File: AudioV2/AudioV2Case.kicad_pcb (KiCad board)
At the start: 2 copper layers, 110 x 110 mm, 265 parts, among them J1601 AUDIO, J1602 V_IN, J1603 15_V_IN, J201 +15/A_GND/-15 out, J202 PD module in (1=GND 2=+12V), Q401 BSS138, Q402 BSS138, SW1601 DEST sense (3PDT 3rd pole, sa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, SW402 PWR SW, SW501 DEST L (PHONE/MUTE/LINE), SW502 DEST R (PHONE/MUTE/LINE), U1601 OPA1656, U1602 OPA1656, U1603 LT1763-3.3, U1605 TPS3307-33, U1606 LT1763-5, U1607 BP5293-50, U1608 OPA1656, U1609 XC8107AC20MR-G, U1610 MCP23017 (UI 0x22), U1611 OPA1656, U201 REC20K-2415DZ, U202 L7809CV +9V, U311 TMUX7612, U312 TMUX7612, U402 PT2314E, U403 BP5293-50 +5V, U501 OPA1652, Y1601 ASFL1-12.288MHZ-EC-T

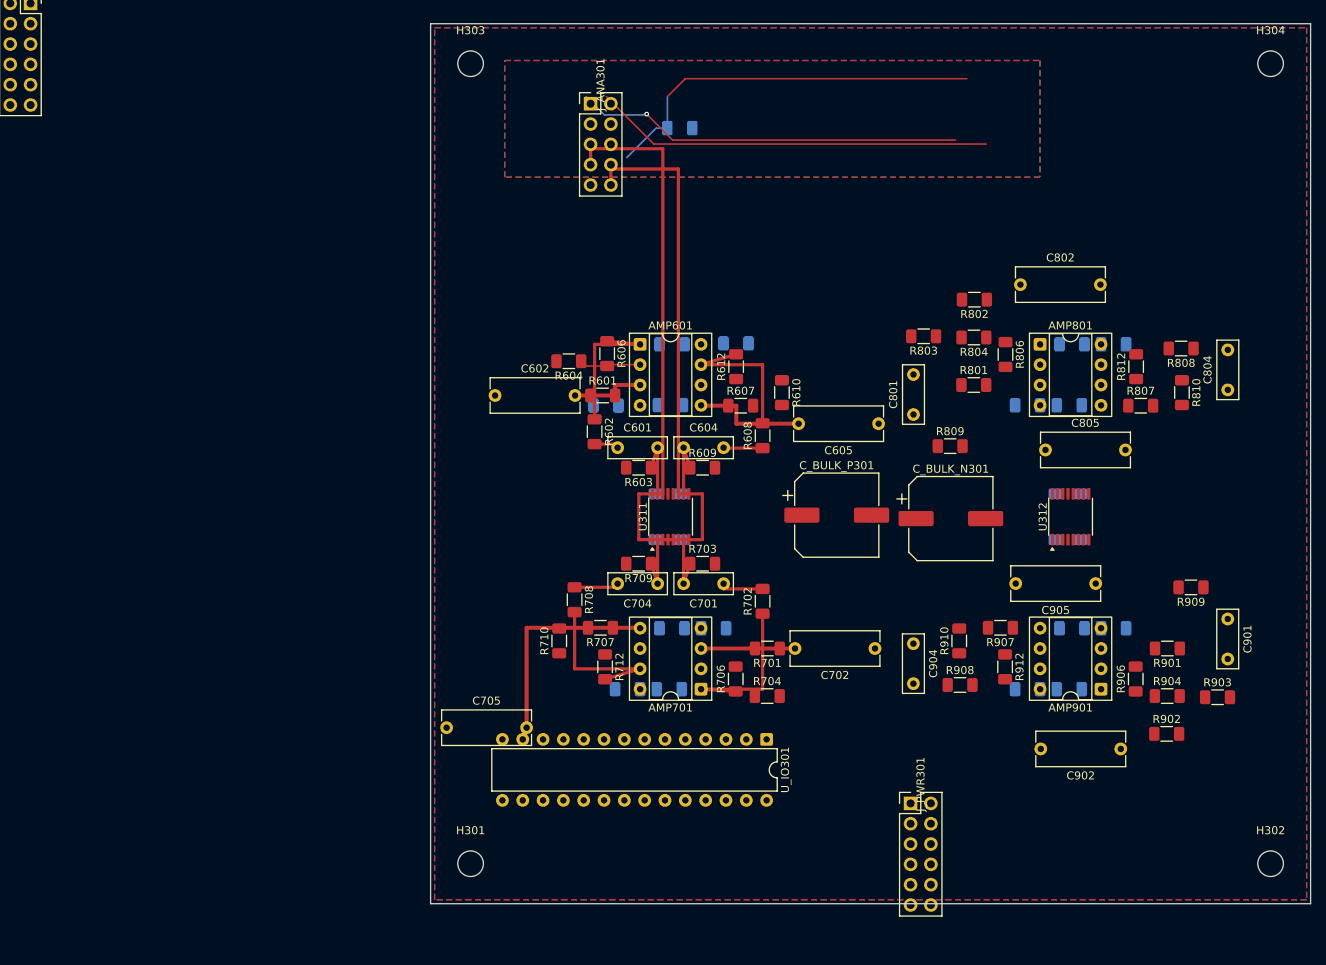
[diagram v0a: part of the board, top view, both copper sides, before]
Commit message: AudioV2: TMUX を 270°（ピン1側=CH1）にし、AmpChannel のスイッチ用デカップを外す
S=各ch出力・D=AMP_SEL に戻し、CH1 配線途中の PCB も取り込む。C607/C610 は D22 の残りなのでシートから削除した。

Co-authored-by: Cursor <cursoragent@cursor.com>
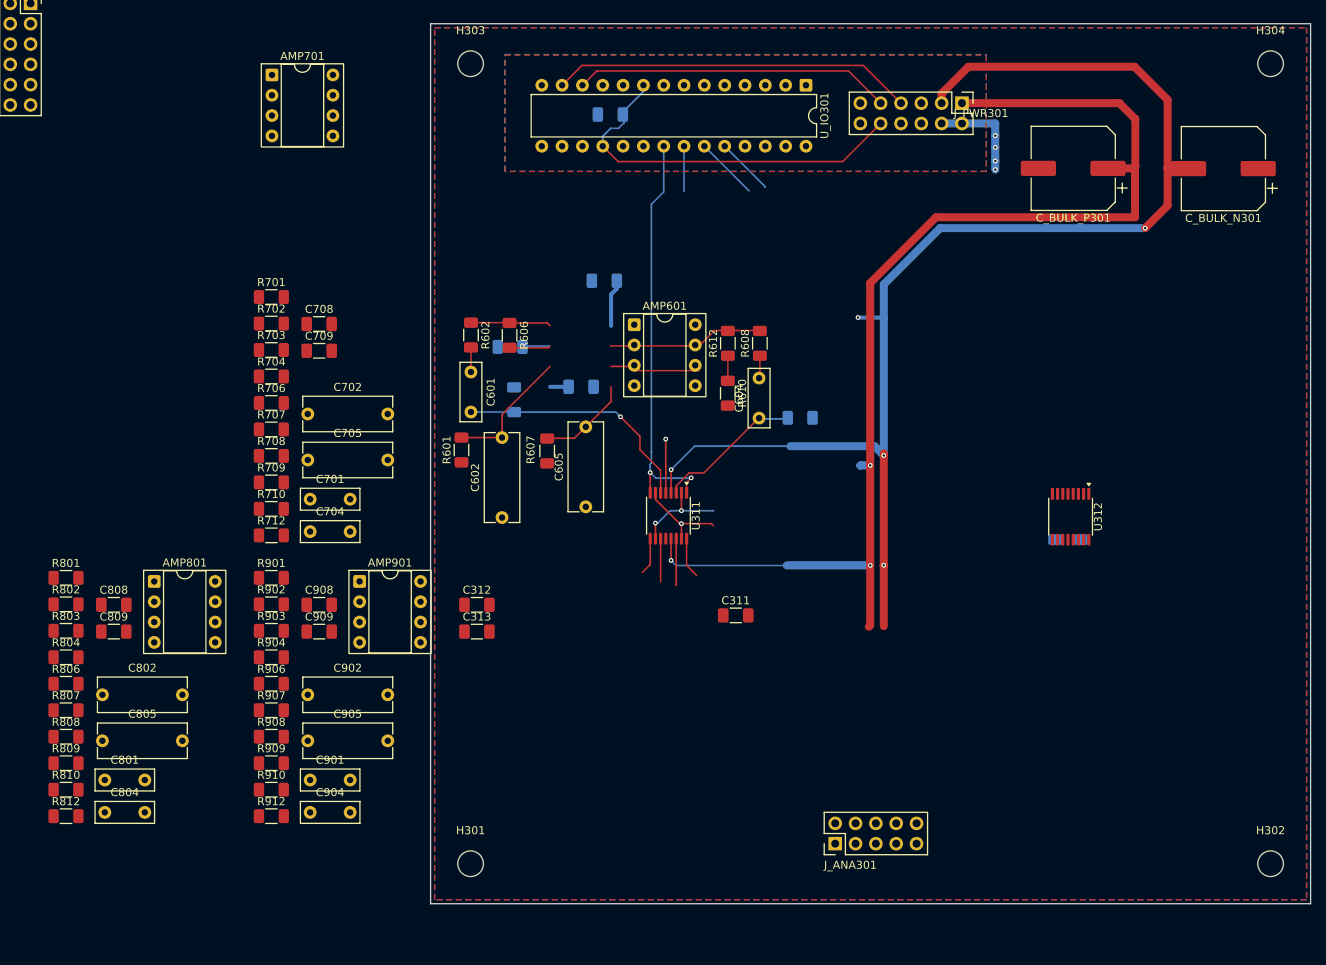
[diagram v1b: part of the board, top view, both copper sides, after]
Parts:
- removed C607, C610, C707, C710, C807, C810, C907, C910: 100nF, Capacitor_SMD:C_1206_3216Metric_Pad1.33x1.80mm_HandSolder
- C311, C312, C313, C708, C709, C808, C809, C908, C909: moved to F.Cu
- R603, R604, R609: moved to B.Cu
- moved C804 150.0 mm to (299.3, 228.6), turned to 0 degrees
- moved R810 148.1 mm to (294.4, 225.7), turned to 0 degrees
- moved R808 147.6 mm to (294.4, 219.1), turned to 0 degrees
- moved R812 145.1 mm to (294.4, 229.1), turned to 0 degrees
- moved R807 139.6 mm to (294.4, 215.8)
- moved C802 125.7 mm to (299.0, 213.9)
- moved R806 124.4 mm to (294.4, 212.5), turned to 0 degrees
- moved C808 124.1 mm to (300.4, 202.6)
- moved C805 123.4 mm to (299.0, 219.6)
- moved R804 120.3 mm to (294.4, 209.2), turned to 0 degrees
- moved R802 119.8 mm to (294.4, 202.6), turned to 0 degrees
- moved R903 118.6 mm to (320.1, 205.9)
- moved C809 117.7 mm to (300.4, 206.0)
- moved R809 117.4 mm to (294.4, 222.4)
- moved R909 117.0 mm to (320.1, 222.4), turned to 0 degrees
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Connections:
- U311 pad 1: /AmpBankSwitch/SEL_CH2 -> /AmpBankSwitch/SEL_CH1
- U311 pad 10: /AmpBankSwitch/CH1_OUT_R -> /AMP_SEL_R
- U311 pad 11: /AMP_SEL_R -> /AmpBankSwitch/CH2_OUT_R
- U311 pad 14: /AMP_SEL_L -> /AmpBankSwitch/CH2_OUT_L
- U311 pad 15: /AmpBankSwitch/CH1_OUT_L -> /AMP_SEL_L
- U311 pad 16: /AmpBankSwitch/SEL_CH1 -> /AmpBankSwitch/SEL_CH2
- U311 pad 2: /AmpBankSwitch/CH2_OUT_R -> /AMP_SEL_R
- U311 pad 3: /AMP_SEL_R -> /AmpBankSwitch/CH1_OUT_R
- U311 pad 6: /AMP_SEL_L -> /AmpBankSwitch/CH1_OUT_L
- U311 pad 7: /AmpBankSwitch/CH2_OUT_L -> /AMP_SEL_L
- U311 pad 8: /AmpBankSwitch/SEL_CH2 -> /AmpBankSwitch/SEL_CH1
- U311 pad 9: /AmpBankSwitch/SEL_CH1 -> /AmpBankSwitch/SEL_CH2
- U312 pad 1: /AmpBankSwitch/SEL_CH4 -> /AmpBankSwitch/SEL_CH3
- U312 pad 10: /AmpBankSwitch/CH3_OUT_R -> /AMP_SEL_R
- U312 pad 11: /AMP_SEL_R -> /AmpBankSwitch/CH4_OUT_R
- U312 pad 14: /AMP_SEL_L -> /AmpBankSwitch/CH4_OUT_L
- U312 pad 15: /AmpBankSwitch/CH3_OUT_L -> /AMP_SEL_L
- U312 pad 16: /AmpBankSwitch/SEL_CH3 -> /AmpBankSwitch/SEL_CH4
- U312 pad 2: /AmpBankSwitch/CH4_OUT_R -> /AMP_SEL_R
- U312 pad 3: /AMP_SEL_R -> /AmpBankSwitch/CH3_OUT_R
- U312 pad 6: /AMP_SEL_L -> /AmpBankSwitch/CH3_OUT_L
- U312 pad 7: /AmpBankSwitch/CH4_OUT_L -> /AMP_SEL_L
- U312 pad 8: /AmpBankSwitch/SEL_CH4 -> /AmpBankSwitch/SEL_CH3
- U312 pad 9: /AmpBankSwitch/SEL_CH3 -> /AmpBankSwitch/SEL_CH4
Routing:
- net /-15V: track 0.00 -> 170.5 mm, vias 0 -> 5
- net /+15V: track 0.00 -> 152.9 mm, vias 0 -> 3
- net /A_GND: track 98.4 -> 19.4 mm, vias 1 -> 5
- net /AMP_SEL_L: track 67.8 -> 11.3 mm, vias 0 -> 1
- net /AMP_SEL_R: track 64.7 -> 12.1 mm, vias 0 -> 2
- net /AmpBankSwitch/SEL_CH1: track 0.00 -> 51.6 mm, vias 0 -> 2
- net /I2C_SDA: track 0.00 -> 45.3 mm
- net /I2C_SCL: track 0.00 -> 39.7 mm
- net Net-(AMP701B-+): track 26.7 -> 0.00 mm
- net /AmpBankSwitch/CH1_OUT_L: track 8.40 -> 30.5 mm, vias 0 -> 1
- net Net-(AMP701-Pad1): track 21.5 -> 0.00 mm
- net Net-(AMP701-Pad7): track 19.8 -> 0.00 mm
- net /AmpBankSwitch/SEL_CH2: track 0.00 -> 15.3 mm
- net Net-(AMP601B--): track 0.00 -> 14.4 mm
- net Net-(AMP701A-+): track 11.7 -> 0.00 mm
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
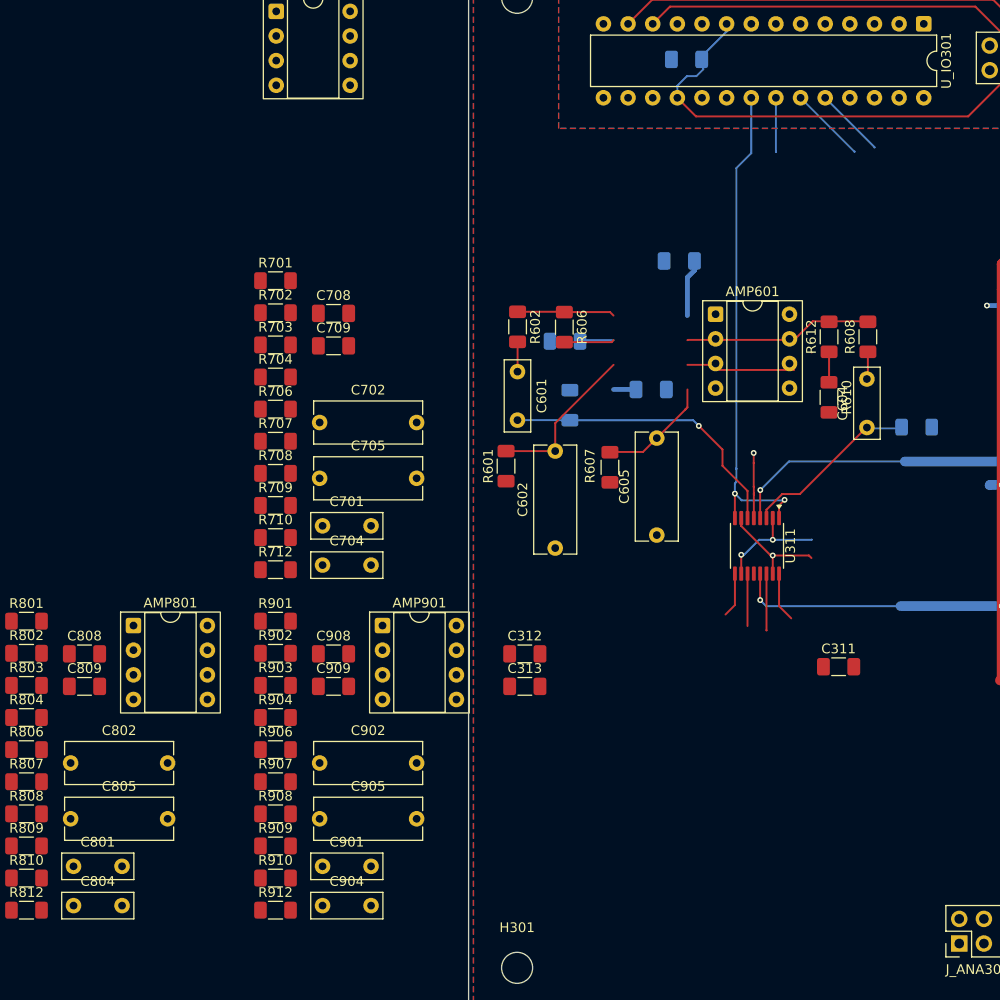
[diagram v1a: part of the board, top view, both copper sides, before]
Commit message: AudioV2: Amp カップリングフィルムを TDK B32529 系統の FP に揃えた
入力1µFは P5/W4.5、出力2.2µFは P5/W7.2。旧 P10 / W2.5 の誤りを直し、PCB も同期。

Co-authored-by: Cursor <cursoragent@cursor.com>
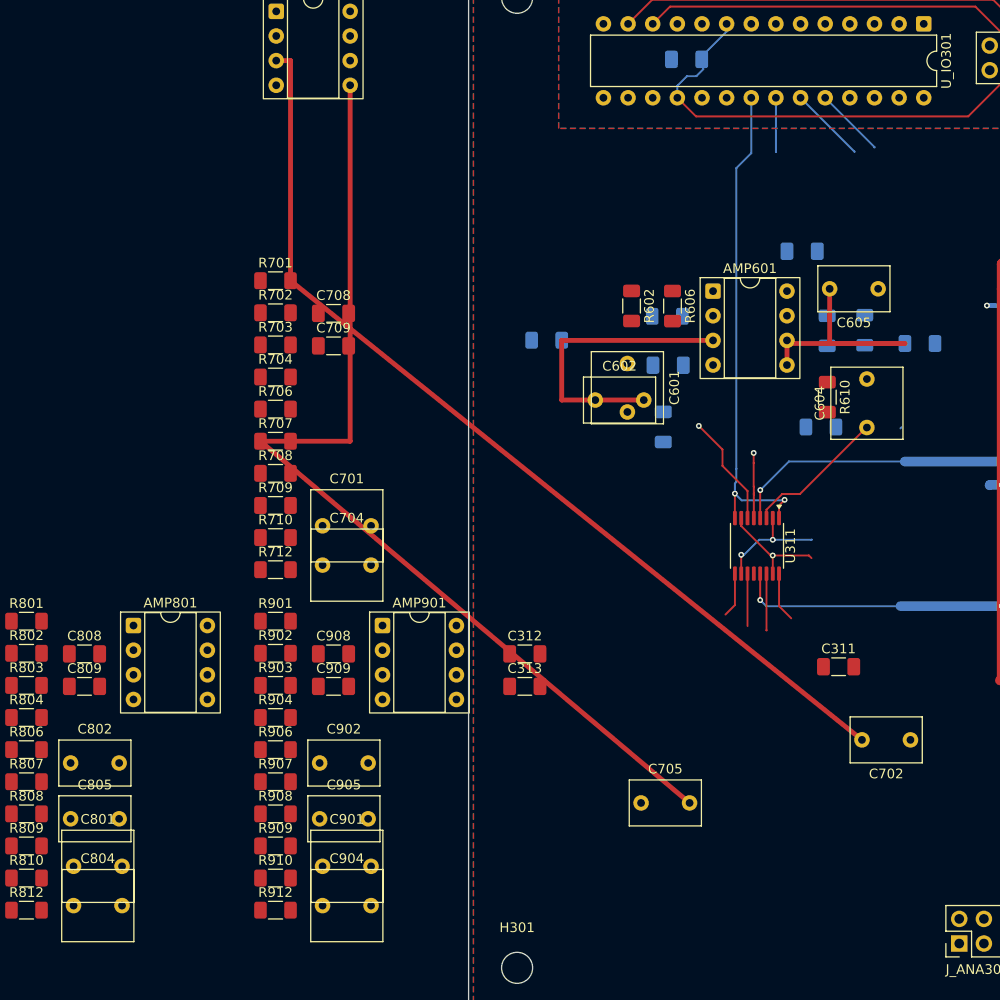
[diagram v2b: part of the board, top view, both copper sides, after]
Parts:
- C601, C604, C701, C704, C801, C804, C901, C904: footprint Capacitor_THT:C_Rect_L7.2mm_W2.5mm_P5.00mm_FKS2_FKP2_MKS2_MKP2 -> C_Rect_L7.2mm_W7.2mm_P5.00mm_FKS2_FKP2_MKS2_MKP2
- C602, C605, C702, C705, C802, C805, C902, C905: footprint Capacitor_THT:C_Rect_L11.0mm_W4.2mm_P10.00mm_MKT -> C_Rect_L7.2mm_W4.5mm_P5.00mm_FKS2_FKP2_MKS2_MKP2
- R601, R607, R608, R612: moved to B.Cu
- moved C702 69.1 mm to (385.6, 211.5), turned to 180 degrees
- moved C705 47.1 mm to (357.8, 218.0)
- moved R607 34.4 mm to (386.5, 170.6), turned to 0 degrees
- moved C605 34.1 mm to (382.2, 165.0), turned to 180 degrees
- moved C602 15.8 mm to (353.1, 176.5), turned to 0 degrees
- moved R601 13.6 mm to (348.1, 170.3), turned to 0 degrees
- moved C608 12.7 mm to (374.4, 161.1), turned to 0 degrees
- moved R602 11.9 mm to (356.8, 166.8)
- moved C601 11.4 mm to (356.4, 172.7)
- moved R606 11.4 mm to (361.0, 166.8)
- moved R604 10.8 mm to (360.5, 167.8)
- moved R603 9.89 mm to (360.1, 179.2), turned to -90 degrees
- moved R609 9.87 mm to (376.3, 179.2), turned to 180 degrees
- moved C609 3.05 mm to (360.6, 172.9), turned to 0 degrees
- moved AMP601 2.39 mm to (365.2, 165.2)
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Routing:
- net Net-(AMP701B-+): track 0.00 -> 103.8 mm
- net Net-(AMP701A-+): track 0.00 -> 99.7 mm
- net Net-(AMP601-Pad7): track 19.4 -> 0.00 mm
- net /AmpBankSwitch/CH1_OUT_L: track 30.5 -> 11.6 mm
- net Net-(AMP601B-+): track 11.9 -> 27.8 mm
- net Net-(AMP601B--): track 14.4 -> 0.00 mm
- net Net-(AMP601A-+): track 16.4 -> 30.2 mm
- net Net-(AMP601-Pad1): track 10.1 -> 0.00 mm
- net Net-(AMP601A--): track 8.64 -> 0.00 mm
- net /+15V: track 152.9 -> 147.0 mm
- net /AmpBankSwitch/CH1_OUT_R: track 18.4 -> 15.0 mm
- net Net-(C601-Pad1): track 3.07 -> 0.00 mm
- net Net-(C604-Pad2): track 2.77 -> 0.07 mm
- net /-15V: track 170.5 -> 168.2 mm
